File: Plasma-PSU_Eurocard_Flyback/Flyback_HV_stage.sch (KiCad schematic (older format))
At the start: 21 parts

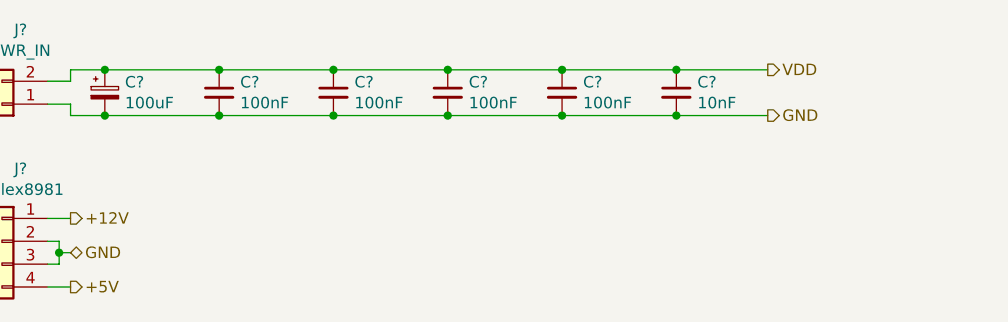
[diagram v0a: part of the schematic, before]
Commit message: Include LTC3786 regulator IC
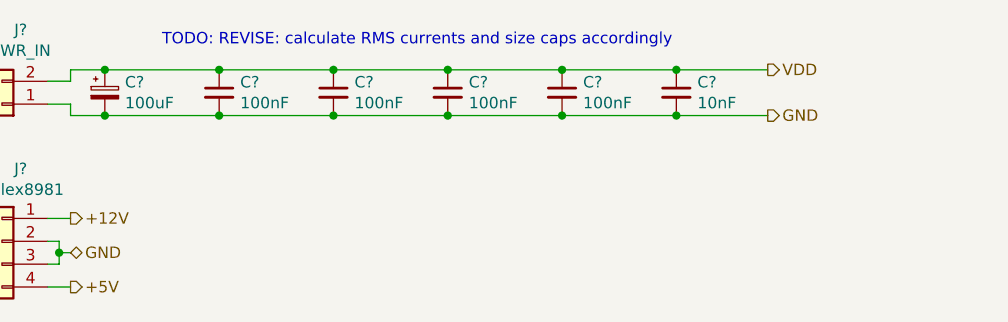
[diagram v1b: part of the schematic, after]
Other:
- note added: "TODO: REVISE: calculate RMS currents and size caps accordingly"
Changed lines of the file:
@@
 $Descr A4 11693 8268
 encoding utf-8
-Sheet 4 4
+Sheet 3 4
 Title "Plasma-PSU_Eurocard_Flyback"
 Date "2020-04-06"
@@
 Text HLabel 4500 2550 1    50   Input ~ 0
 ENBL
+Text Notes 1750 800  0    50   ~ 0
+TODO: REVISE: calculate RMS currents and size caps accordingly
 $EndSCHEMATC

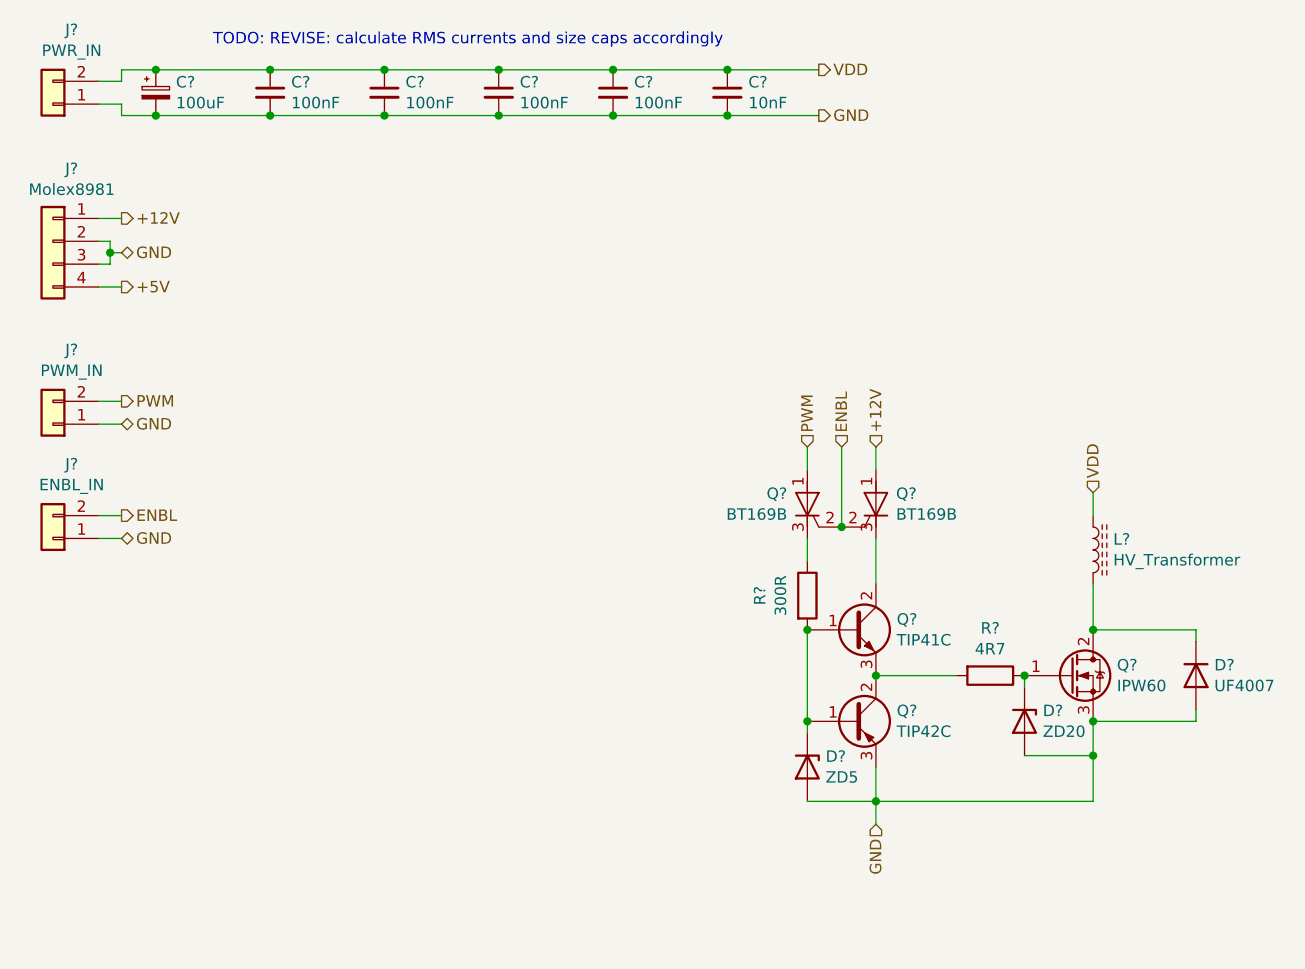
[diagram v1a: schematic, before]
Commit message: Block diagram, Connectivity, Isolation
- First page reservered for block diagram
- Connectors moved to separate sheet
- Opto-isolators for signal inputs on HV board
- Fuse added to SMPS
- Pinheader for Arduino pin-out, UART, I2C, SPI
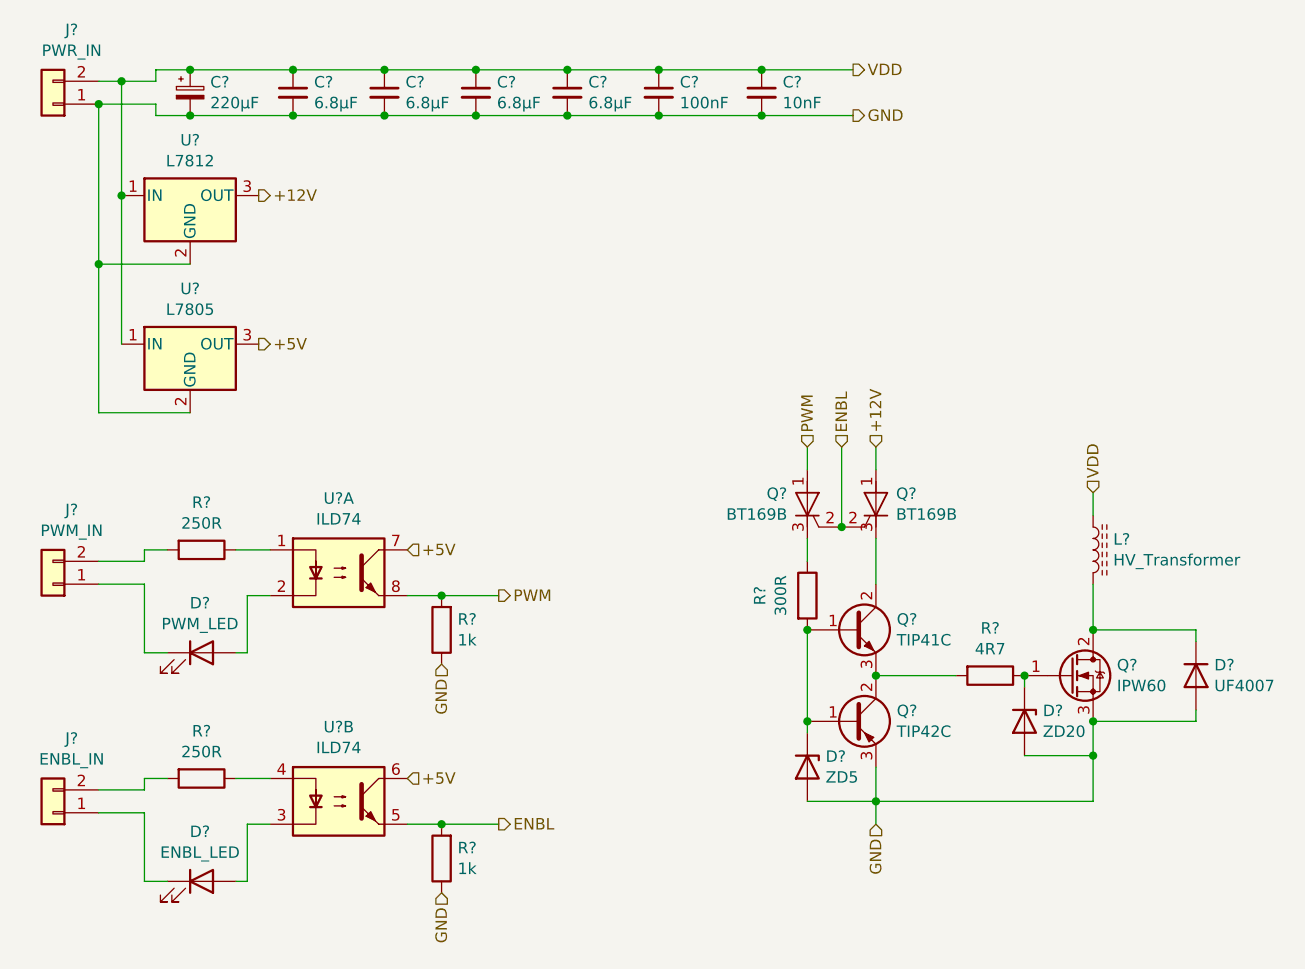
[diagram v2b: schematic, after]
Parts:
- removed C? (x2): 100nF, symbol Device:C_Small
- removed J?: Molex8981, symbol Connector_Generic:Conn_01x04
- added C? (x3): 6.8µF, symbol Device:C_Small
- added D?: PWM_LED, symbol Device:LED
- added D?: ENBL_LED, symbol Device:LED
- added R? (x2): 250R, symbol Device:R
- added R? (x2): 1k, symbol Device:R
- added U?: L7812, symbol Regulator_Linear:L7812
- added U?: L7805, symbol Regulator_Linear:L7805
- added U? (x2): ILD74, symbol Isolator:ILD74
- C?: value 100nF -> 6.8µF
- C?: value 100uF -> 220µF
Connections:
- net +12V: now also U?.3 (OUT)
- net +5V: now also U?.3 (OUT), U?.6, U?.7
- net ENBL: now also R?.2, U?.5; no longer J?.2 (Pin_2)
- net GND: now also C?.2, C?.2, C?.2, R?.1, R?.1, U?.2 (GND), U?.2 (GND); no longer J?.1 (Pin_1), J?.1 (Pin_1)
- net PWM: now also R?.2, U?.8; no longer J?.2 (Pin_2)
- net VDD: now also C?.1, C?.1, C?.1, U?.1 (IN), U?.1 (IN)
- new net: D?.1 (K), J?.1 (Pin_1) (x2)
- new net: J?.2 (Pin_2), R?.2 (x2)
- new net: R?.1, U?.1
- new net: D?.2 (A), U?.2
- new net: D?.2 (A), U?.3
- new net: R?.1, U?.4
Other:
- note removed: "TODO: REVISE: calculate RMS currents and size caps accordingly"
- moved on the sheet: C?, J?

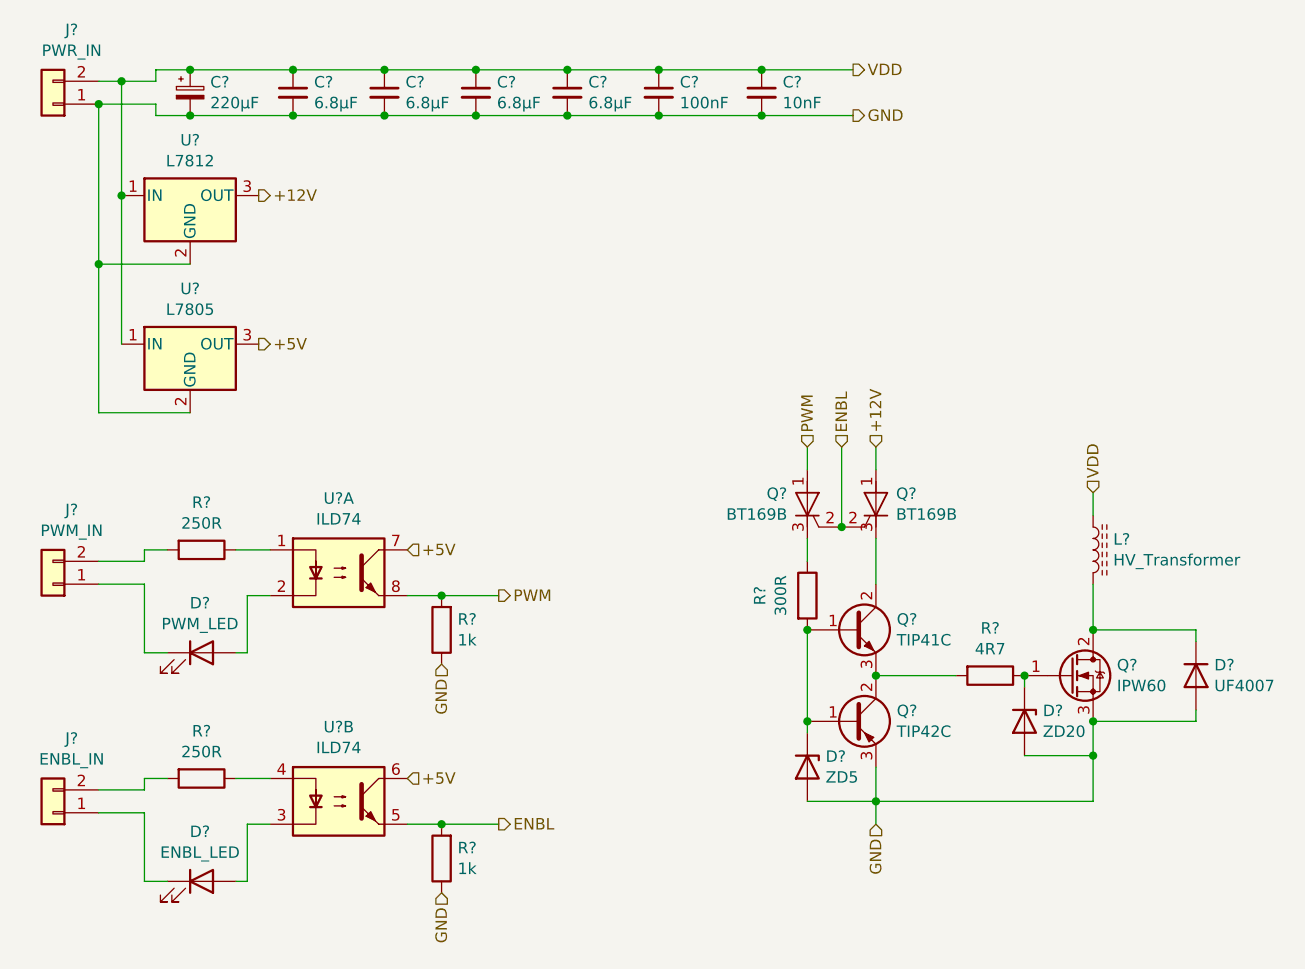
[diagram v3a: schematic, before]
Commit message: Footprints added
All footprints included, except:
- Boost Inductor
- 60A fuse holder
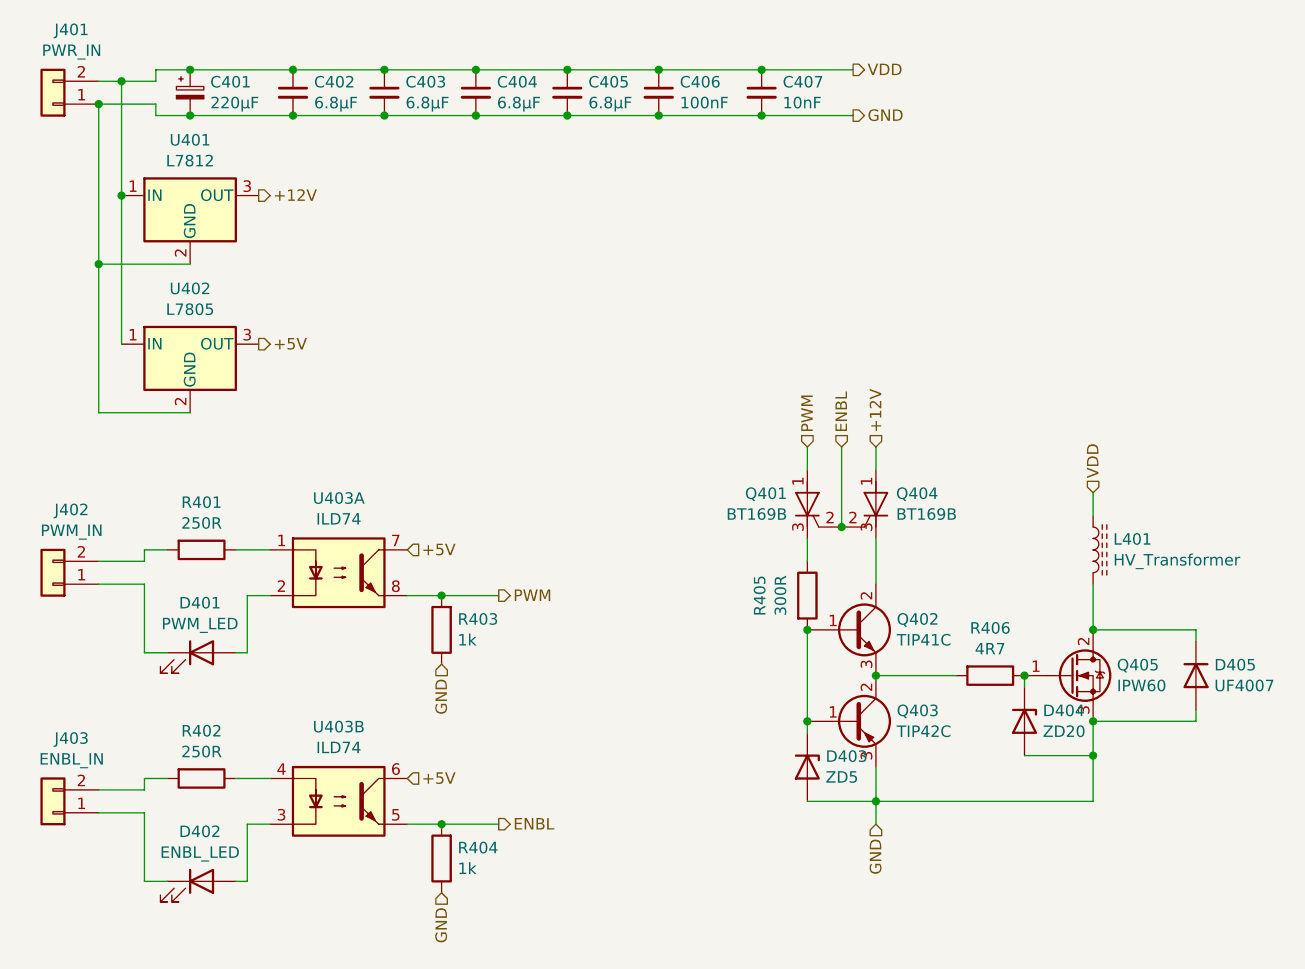
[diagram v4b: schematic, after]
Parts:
- C401: renamed from C?; footprint (none) -> Capacitor_THT:CP_Radial_D8.0mm_P3.50mm
- C402, C403, C404, C405: renamed from C?; footprint (none) -> Capacitor_THT:C_Disc_D6.0mm_W2.5mm_P5.00mm
- C406: renamed from C?; footprint (none) -> Capacitor_SMD:C_1206_3216Metric
- C407: renamed from C?; footprint (none) -> Capacitor_SMD:C_0805_2012Metric
- D401, D402: renamed from D?; footprint (none) -> LED_SMD:LED_0603_1608Metric
- J401: renamed from J?; footprint (none) -> TerminalBlock_Phoenix:TerminalBlock_Phoenix_MKDS-3-2-5.08_1x02_P5.08mm_Horizontal
- J402, J403: renamed from J?; footprint (none) -> Connector_PinHeader_2.54mm:PinHeader_1x02_P2.54mm_Vertical
- R401, R402, R403, R404: renamed from R?; footprint (none) -> Resistor_THT:R_Axial_DIN0207_L6.3mm_D2.5mm_P7.62mm_Horizontal
- U401, U402: renamed from U?; footprint (none) -> Package_TO_SOT_THT:TO-220-3_Horizontal_TabDown
- U403: renamed from U?; footprint (none) -> Package_DIP:DIP-8_W7.62mm
- gave numbers to parts that had none: 11
